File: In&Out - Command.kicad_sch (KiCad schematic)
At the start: 0 parts

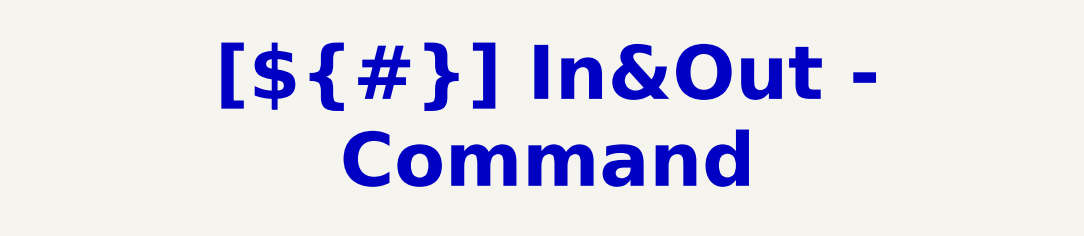
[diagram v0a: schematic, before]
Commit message: [Project][Added] CI/CD environment
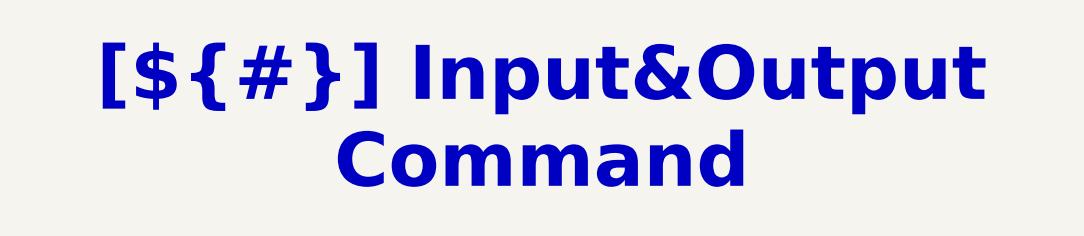
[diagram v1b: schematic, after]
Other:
- title: In&Out - Command -> Input&Output Command
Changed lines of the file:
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@@
 (kicad_sch
-	(version 20260306)
+	(version 20250114)
 	(generator "eeschema")
-	(generator_version "10.0")
+	(generator_version "9.0")
 	(paper "A4")
 	(title_block
-		(title "In&Out - Command")
+		(title "Input&Output Command")
 		(date "2025-01-12")
 		(rev "${REVISION}")
@@
 	(text_box "[${#}] ${TITLE}"
 		(exclude_from_sim no)
-		(at 97.79 15.24 0)
-		(size 104.14 12.7)
+		(at 88.9 15.24 0)
+		(size 120.65 12.7)
 		(margins 4.4999 4.4999 4.4999 4.4999)
 		(stroke

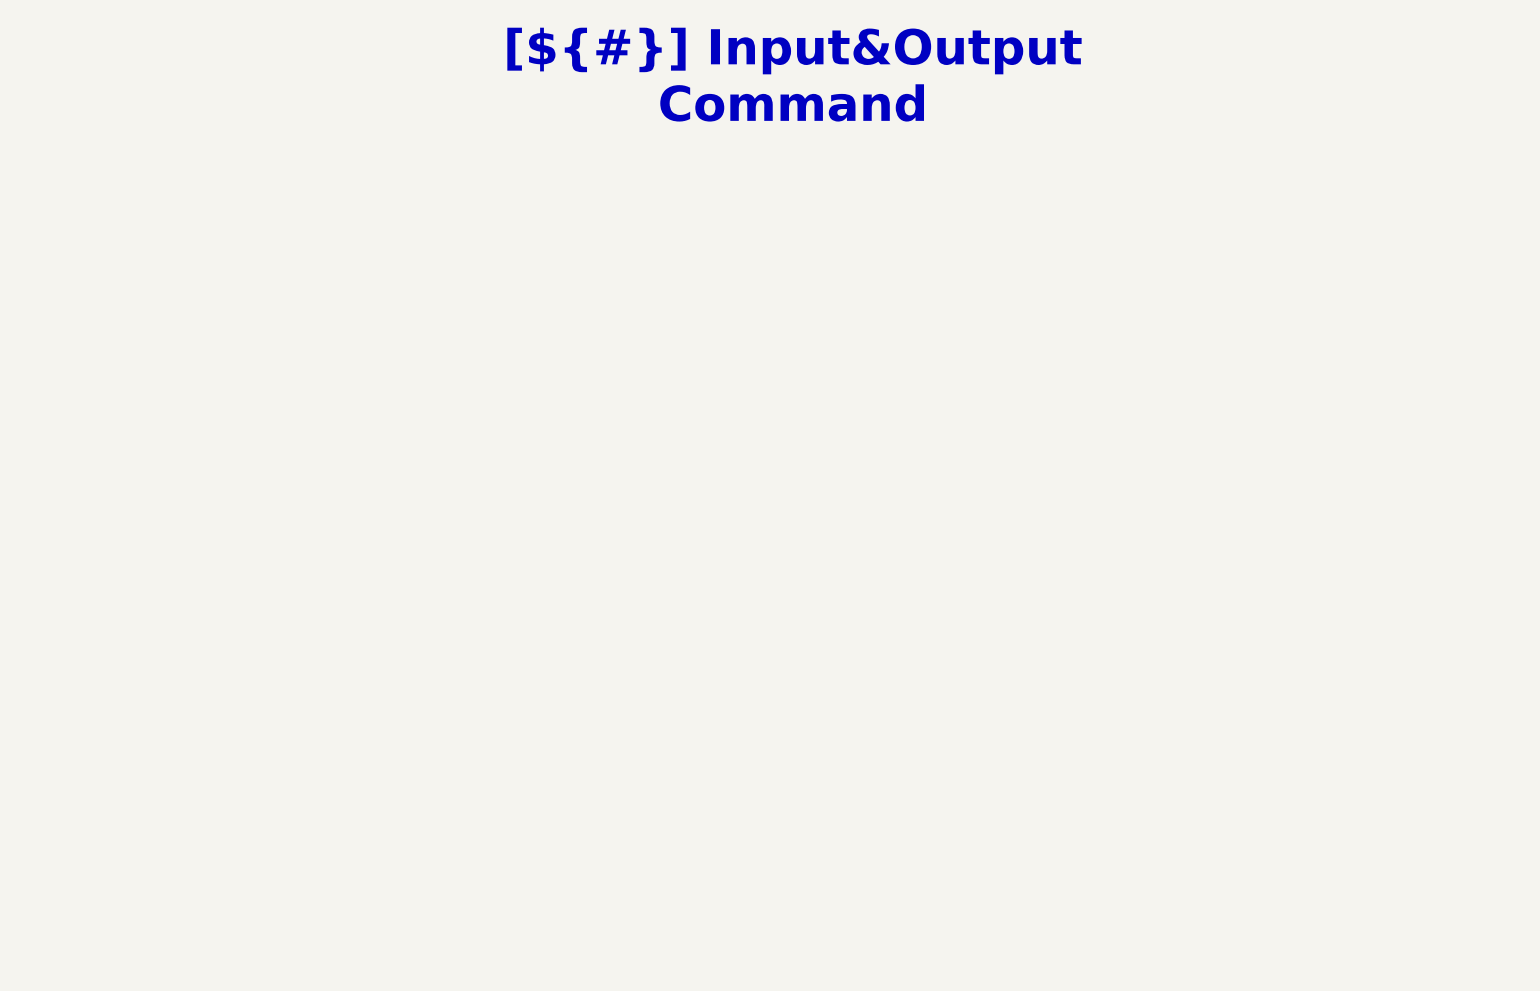
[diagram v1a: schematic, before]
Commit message: [Schematic][Add] In&Out - Command, add schematic
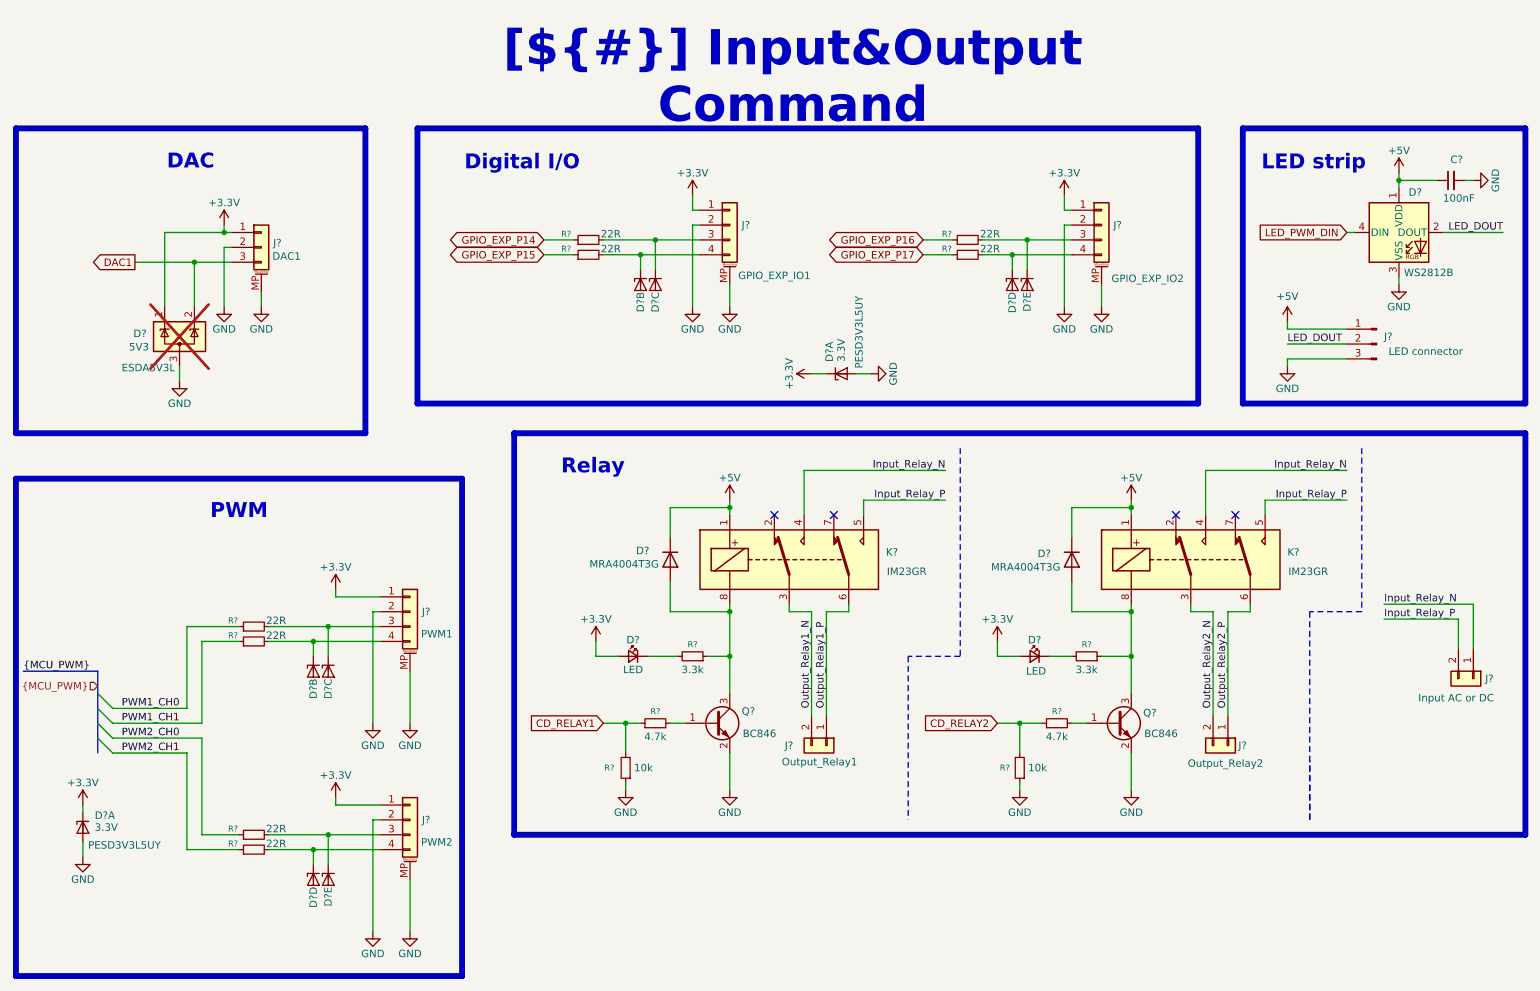
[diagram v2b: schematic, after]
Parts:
- added C?: 100nF, Capacitor_SMD:C_0603_1608Metric_Pad1.08x0.95mm_HandSolder, symbol Device:C_Small
- added D? (x2): *, Diode_SMD:D_SMA, symbol Diode:MRA4004T3G
- added D? (x10): 3.3V, Package_TO_SOT_SMD:SOT-363_SC-70-6, symbol Power_Protection:PESD3V3L5UY
- added D? (x2): 5V, LED_SMD:LED_0805_2012Metric_Pad1.15x1.40mm_HandSolder, symbol Device:LED_Small
- added D?: 5V, LED_SMD:LED_WS2812B_PLCC4_5.0x5.0mm_P3.2mm, symbol LED:WS2812B
- added D?: 5V3, Package_TO_SOT_SMD:SOT-23-3, symbol Power_Protection:ESDA5V3L
- added J? (x4): *, Connector_JST:JST_PH_S4B-PH-SM4-TB_1x04-1MP_P2.00mm_Horizontal, symbol Connector_Generic_MountingPin:Conn_01x04_MountingPin
- added J? (x3): *, P_Phoenix:PHOENIX_1x2_1928767, symbol P_Phoenix_Connector:Conn_01x02
- added J?: *, Connector_PinHeader_2.54mm:PinHeader_1x03_P2.54mm_Vertical, symbol Connector:Conn_01x03_Pin
- added J?: *, Connector_JST:JST_PH_S3B-PH-SM4-TB_1x03-1MP_P2.00mm_Horizontal, symbol Connector_Generic_MountingPin:Conn_01x03_MountingPin
- added K? (x2): 5V, Relay_SMD:Relay_DPDT_AXICOM_IMSeries_JLeg, symbol Relay:IM23
- added Q? (x2): *, Package_TO_SOT_SMD:SOT-23, symbol Transistor_BJT:BC846
- added R? (x2): 10k, Resistor_SMD:R_0603_1608Metric_Pad0.98x0.95mm_HandSolder, symbol Device:R_Small
- added R? (x8): 22R, Resistor_SMD:R_0603_1608Metric_Pad0.98x0.95mm_HandSolder, symbol Device:R_Small
- added R? (x2): 3.3k, Resistor_SMD:R_0603_1608Metric_Pad0.98x0.95mm_HandSolder, symbol Device:R_Small
- added R? (x2): 4.7k, Resistor_SMD:R_0603_1608Metric_Pad0.98x0.95mm_HandSolder, symbol Device:R_Small
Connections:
- new net: D?.4 (K3), J?.3 (Pin_3), R?.2 (x2)
- new net: D?.3 (K2), J?.4 (Pin_4), R?.2 (x2)
- new net: D?.5 (K4), J?.4 (Pin_4), R?.2 (x2)
- new net: D?.6 (K5), J?.3 (Pin_3), R?.2 (x2)
- new net: D?.2 (A), K?.8, Q?.3 (C), R?.1 (x2)
- new net: D?.1 (K), R?.2 (x2)
- new net: Q?.1 (B), R?.2 (x2)
- new net +3.3V: D?.1 (K), D?.1 (K1), D?.1 (K1), D?.2 (A), D?.2 (A), J?.1 (Pin_1), J?.1 (Pin_1), J?.1 (Pin_1), J?.1 (Pin_1), J?.1 (Pin_1)
- new net +5V: C?.1, D?.1 (K), D?.1 (K), D?.1 (VDD), J?.1 (Pin_1), K?.1, K?.1
- new net CD_RELAY1: R?.1, R?.2
- new net CD_RELAY2: R?.1, R?.2
- new net DAC1: D?.2 (K), J?.3 (Pin_3)
- new net GND: C?.2, D?.2 (A), D?.2 (A), D?.3 (A), D?.3 (VSS), J?.2 (Pin_2), J?.2 (Pin_2), J?.2 (Pin_2), J?.2 (Pin_2), J?.2 (Pin_2), J?.3 (Pin_3), J?.MP (MountPin), J?.MP (MountPin), J?.MP (MountPin), J?.MP (MountPin), J?.MP (MountPin), Q?.2 (E), Q?.2 (E), R?.1, R?.1
- new net GPIO_EXP_P14: R?.1
- new net GPIO_EXP_P15: R?.1
- new net GPIO_EXP_P16: R?.1
- new net GPIO_EXP_P17: R?.1
- new net Input_Relay_N: J?.1 (Pin_1), K?.4, K?.4
- new net Input_Relay_P: J?.2 (Pin_2), K?.5, K?.5
- new net LED_DOUT: D?.2 (DOUT), J?.2 (Pin_2)
- new net LED_PWM_DIN: D?.4 (DIN)
- new net Output_Relay1_N: J?.2 (Pin_2), K?.3
- new net Output_Relay1_P: J?.1 (Pin_1), K?.6
- new net Output_Relay2_N: J?.2 (Pin_2), K?.3
- new net Output_Relay2_P: J?.1 (Pin_1), K?.6
- new net PWM1_CH0: R?.1
- new net PWM1_CH1: R?.1
- new net PWM2_CH0: R?.1
- new net PWM2_CH1: R?.1
- no-connect marks 0 -> 4

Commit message: [Schematic][Modify] Annotation of all  the components
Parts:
- gave numbers to parts that had none: 36

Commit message: [Schematic][Modify] Annotation of all  the components
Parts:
- renumbered D28 to D21, D24 to D22, D22 to D23, D25 to D24, D27 to D25, D23 to D26, D26 to D27, D21 to D28, J17 to J14, J19 to J15, J14 to J16, J21 to J17, J15 to J18, J22 to J19, J18 to J20, J20 to J21, J16 to J22, R44 to R40, R49 to R41, R45 to R42, R50 to R43, R40 to R44, R41 to R45, R48 to R46, R53 to R47, R47 to R48, R52 to R49, R46 to R50, R42 to R52, R43 to R53

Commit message: [Schematic][Modify] Monification of simulation models
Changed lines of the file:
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@@
 		(dnp no)
 		(property "Reference" "J20"
-			(at 147.828 135.89 90)
+			(at 147.066 135.89 90)
 			(effects
 				(font
@@
 			)
 		)
-		(property "Sim.Device" "NPN"
-			(at 135.89 132.08 0)
+		(property "PartNumber" "BC846"
+			(at 143.51 133.858 0)
 			(effects
 				(font
 					(size 1.27 1.27)
 				)
-				(hide yes)
 			)
 		)
-		(property "Sim.Pins" "1=B 2=E 3=C"
+		(property "PackageReference" "SOT-23"
 			(at 135.89 132.08 0)
 			(effects
@@
 			)
 		)
-		(property "PartNumber" "BC846"
-			(at 143.51 133.858 0)
-			(effects
-				(font
-					(size 1.27 1.27)
-				)
-			)
-		)
-		(property "PackageReference" "SOT-23"
+		(property "Manufacturer" "Nexperia"
 			(at 135.89 132.08 0)
 			(effects
@@
 			)
 		)
-		(property "Manufacturer" "Nexperia"
+		(property "Comment" "NPN"
 			(at 135.89 132.08 0)
 			(effects
@@
 			)
 		)
-		(property "Comment" "NPN"
+		(property "Sim.Library" ".\\"
 			(at 135.89 132.08 0)
 			(effects
@@
 			)
 		)
+		(property "Sim.Library" ".\\"
+			(at 252.73 48.26 0)
+			(effects
+				(font
+					(size 1.27 1.27)
+				)
+				(hide yes)
+			)
+		)
 		(pin "1"
 		)
@@
 			)
 		)
+		(property "Sim.Library" ".\\"
+			(at 44.45 66.04 0)
+			(effects
+				(font
+					(size 1.27 1.27)
+				)
+				(hide yes)
+			)
+		)
 		(pin "3"
 		)
@@
 			)
 		)
+		(property "Sim.Library" ".\\"
+			(at 67.31 158.75 0)
+			(effects
+				(font
+					(size 1.27 1.27)
+				)
+				(hide yes)
+			)
+		)
 		(pin "3"
 		)
@@
 			)
 		)
+		(property "Sim.Library" ".\\"
+			(at 217.17 104.14 0)
+			(effects
+				(font
+					(size 1.27 1.27)
+				)
+				(hide yes)
+			)
+		)
 		(pin "1"
 		)
@@
 			)
 		)
+		(property "Sim.Library" ".\\"
+			(at 67.31 123.19 0)
+			(effects
+				(font
+					(size 1.27 1.27)
+				)
+				(hide yes)
+			)
+		)
 		(pin "3"
 		)
@@
 			)
 		)
+		(property "Sim.Library" ".\\"
+			(at 27.94 149.86 0)
+			(effects
+				(font
+					(size 1.27 1.27)
+				)
+				(hide yes)
+			)
+		)
 		(pin "3"
 		)
@@
 			)
 		)
+		(property "Sim.Library" ".\\"
+			(at 69.85 123.19 0)
+			(effects
+				(font
+					(size 1.27 1.27)
+				)
+				(hide yes)
+			)
+		)
 		(pin "3"
 		)
@@
 			)
 		)
+		(property "Sim.Library" ".\\"
+			(at 69.85 158.75 0)
+			(effects
+				(font
+					(size 1.27 1.27)
+				)
+				(hide yes)
+			)
+		)
 		(pin "3"
 		)
@@
 			)
 		)
-		(property "Sim.Device" "NPN"
-			(at 204.47 132.08 0)
+		(property "PartNumber" "BC846"
+			(at 212.09 133.858 0)
 			(effects
 				(font
 					(size 1.27 1.27)
 				)
-				(hide yes)
 			)
 		)
-		(property "Sim.Pins" "1=B 2=E 3=C"
+		(property "PackageReference" "SOT-23"
 			(at 204.47 132.08 0)
 			(effects
@@
 			)
 		)
-		(property "PartNumber" "BC846"
-			(at 212.09 133.858 0)
-			(effects
-				(font
-					(size 1.27 1.27)
-				)
-			)
-		)
-		(property "PackageReference" "SOT-23"
+		(property "Manufacturer" "Nexperia"
 			(at 204.47 132.08 0)
 			(effects
@@
 			)
 		)
-		(property "Manufacturer" "Nexperia"
+		(property "Comment" "NPN"
 			(at 204.47 132.08 0)
 			(effects
@@
 			)
 		)
-		(property "Comment" "NPN"
+		(property "Sim.Library" ".\\"
 			(at 204.47 132.08 0)
 			(effects
